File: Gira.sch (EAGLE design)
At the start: 20 parts, among them IC1 MEGA8-PTQFP

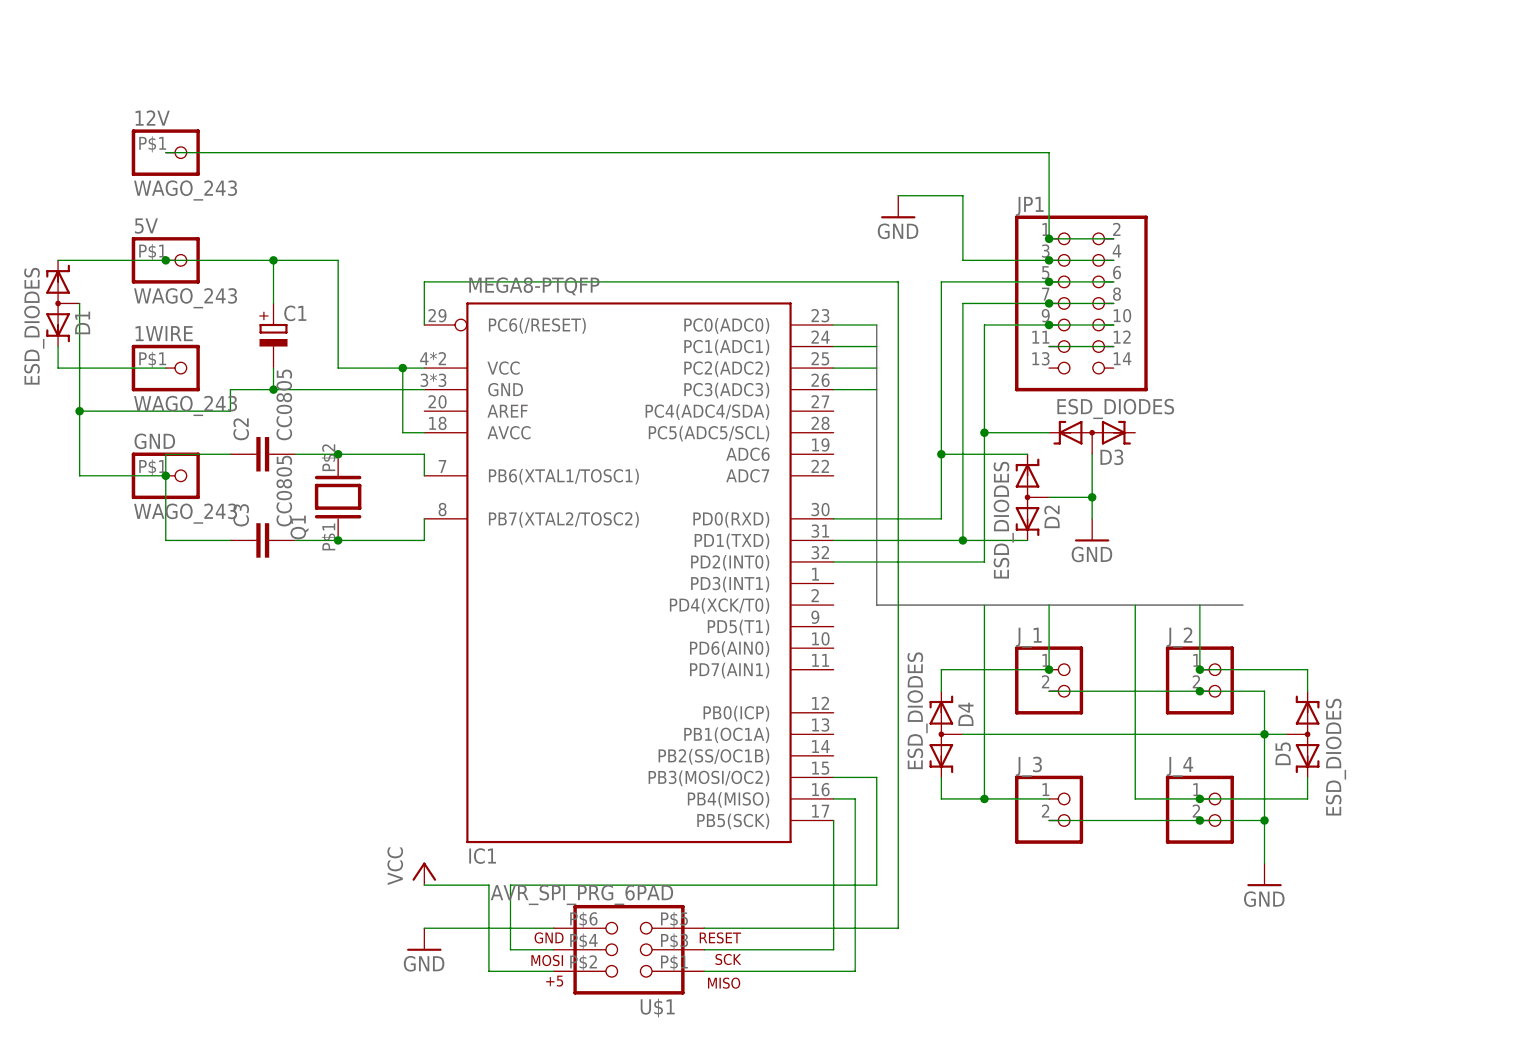
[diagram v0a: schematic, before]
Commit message: Additional ground, I²C bus, input for light measurement
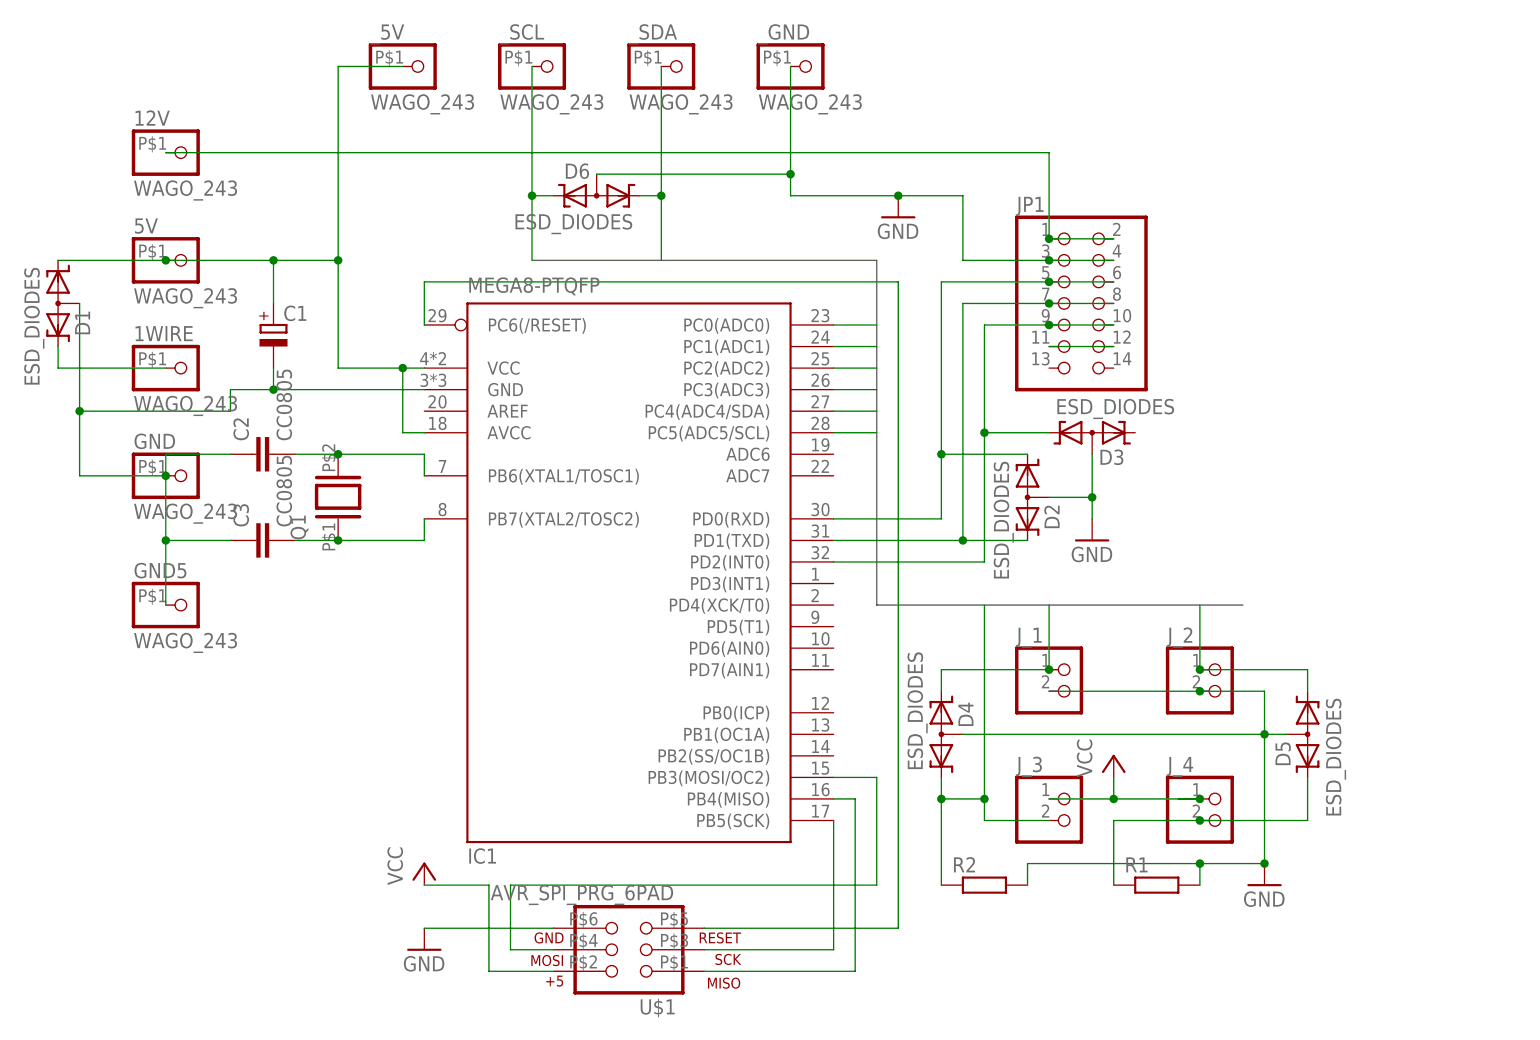
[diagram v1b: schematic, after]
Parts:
- added D6: ESD_DIODES, common:ESD_DIODES
- added GND5, _5V, _GND, _SCL, _SDA: WAGO_243, common:WAGO_243
- added R1, R2: (no value), resistor:R-EU_R0603
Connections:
- new net N$6: D5.K2, J_4.2, R1.1
- new net SCL: D6.K2, IC1.PC5(ADC5/SCL), _SCL.1
- new net SDA: D6.K1, IC1.PC4(ADC4/SDA), _SDA.1
- new net VCC: J_3.1, J_4.1
- net 5V: now also _5V.1
- net B3: now also J_3.2, R2.1; no longer J_3.1
- net B4: no longer D5.K2, J_4.1
- net GND: now also D6.AA, GND5.1, R1.2, R2.2, _GND.1; no longer J_3.2, J_4.2

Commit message: Update Gira
min 0.3mm
Klemmen gedreht
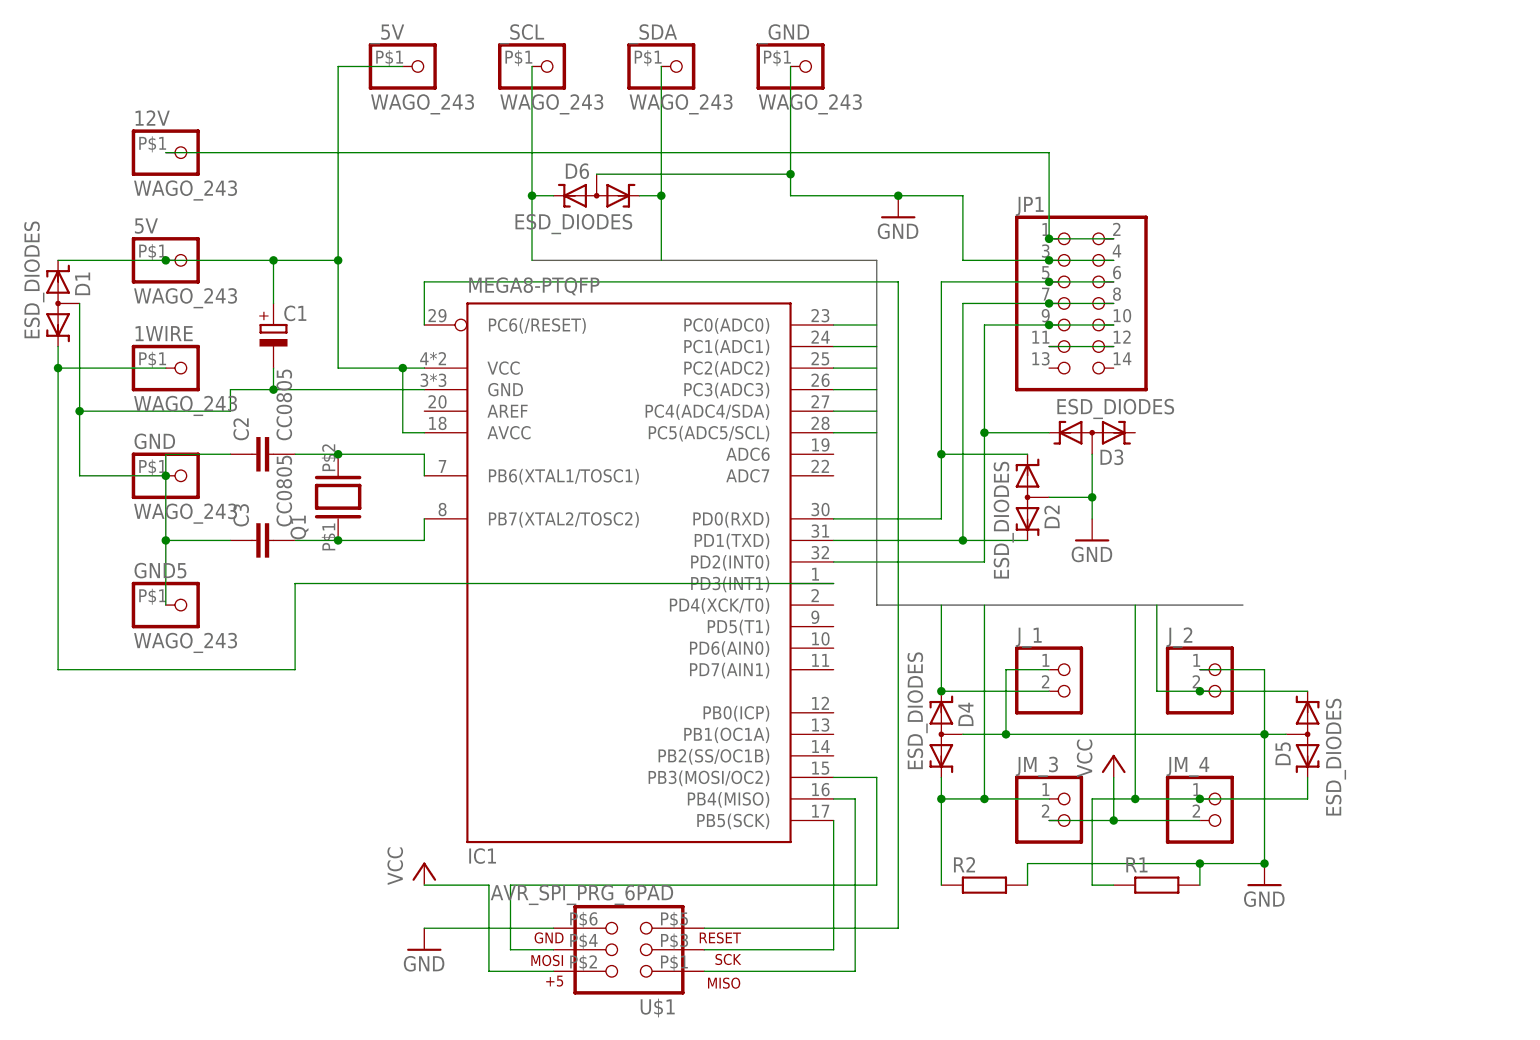
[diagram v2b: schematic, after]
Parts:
- removed J_3, J_4: (no value), pinhead:PINHD-1X2
- added JM_3, JM_4: (no value), common:PINHD-1X2LEVER
- J_1, J_2: device pinhead:PINHD-1X2 -> common:PINHD-1X2LEVER
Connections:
- removed net N$6: D5.K2, J_4.2, R1.1
- removed net VCC: J_3.1, J_4.1
- net 5V: now also D1.K2, JM_3.2, JM_4.2; no longer D1.K1
- net B1: now also J_1.2; no longer J_1.1
- net B2: now also J_2.2; no longer J_2.1
- net B3: now also JM_3.1; no longer J_3.2
- net B4: now also D5.K2, JM_4.1, R1.1
- net GND: now also J_1.1, J_2.1; no longer J_1.2, J_2.2
- net N$2: now also D1.K1, IC1.PD3(INT1); no longer D1.K2
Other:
- moved on the sheet: D1

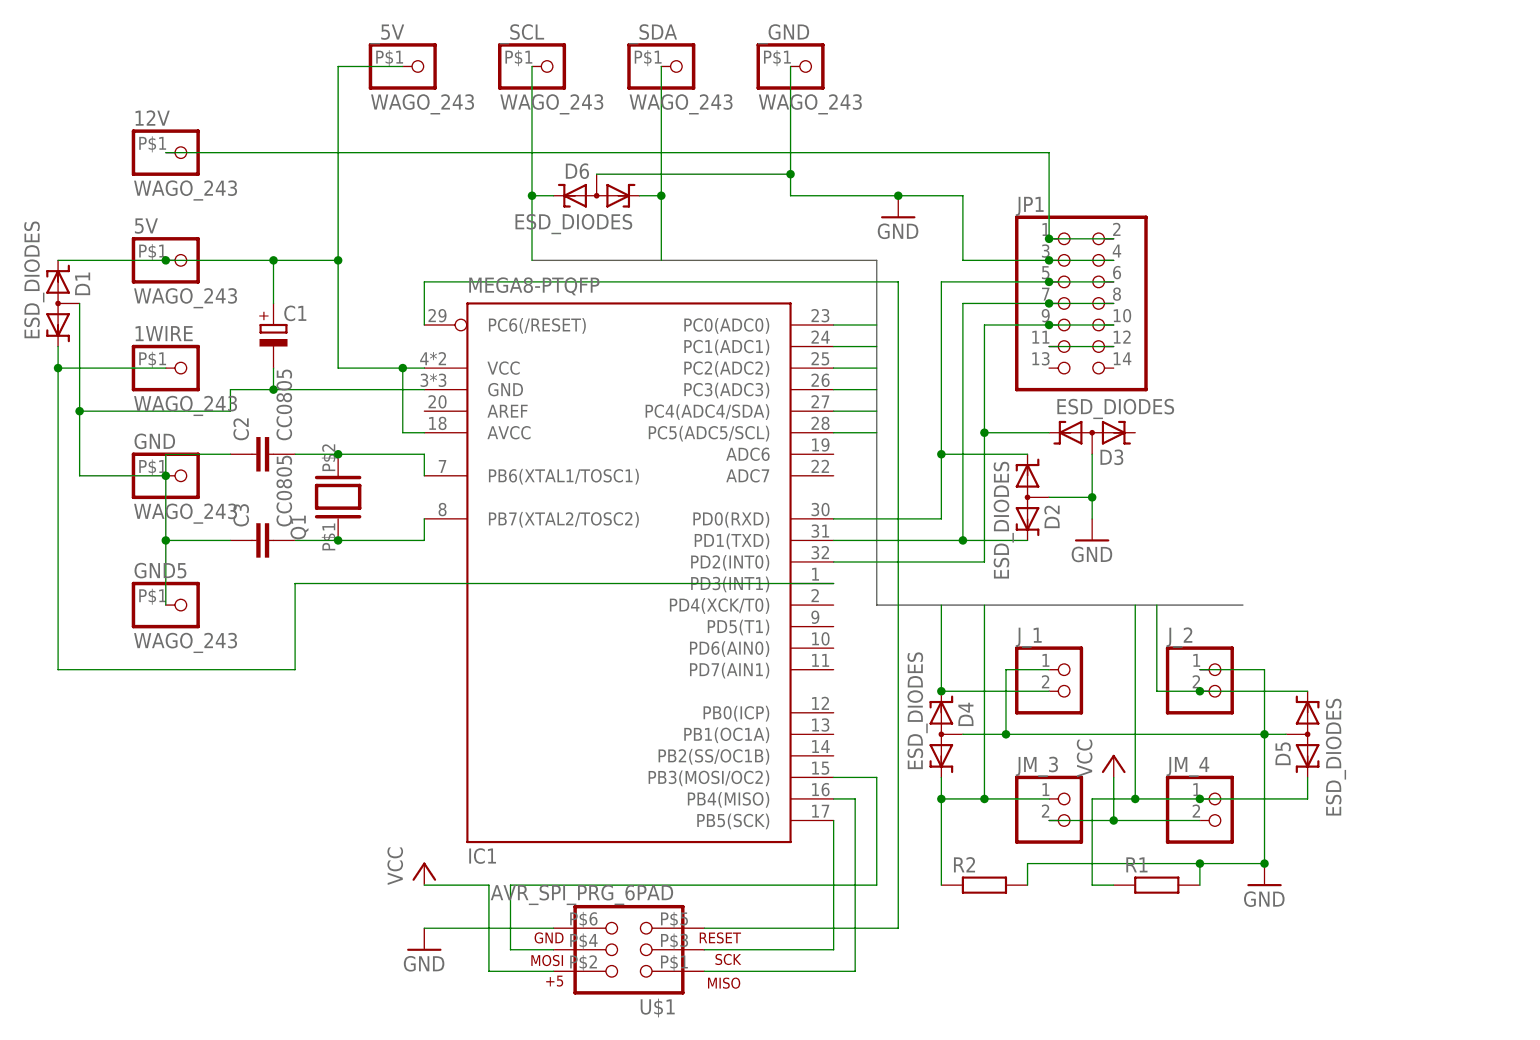
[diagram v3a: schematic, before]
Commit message: V2.1
* Umstellung auf 3.3V (aus dem Rauchmelder)
* keine Pullups am Port
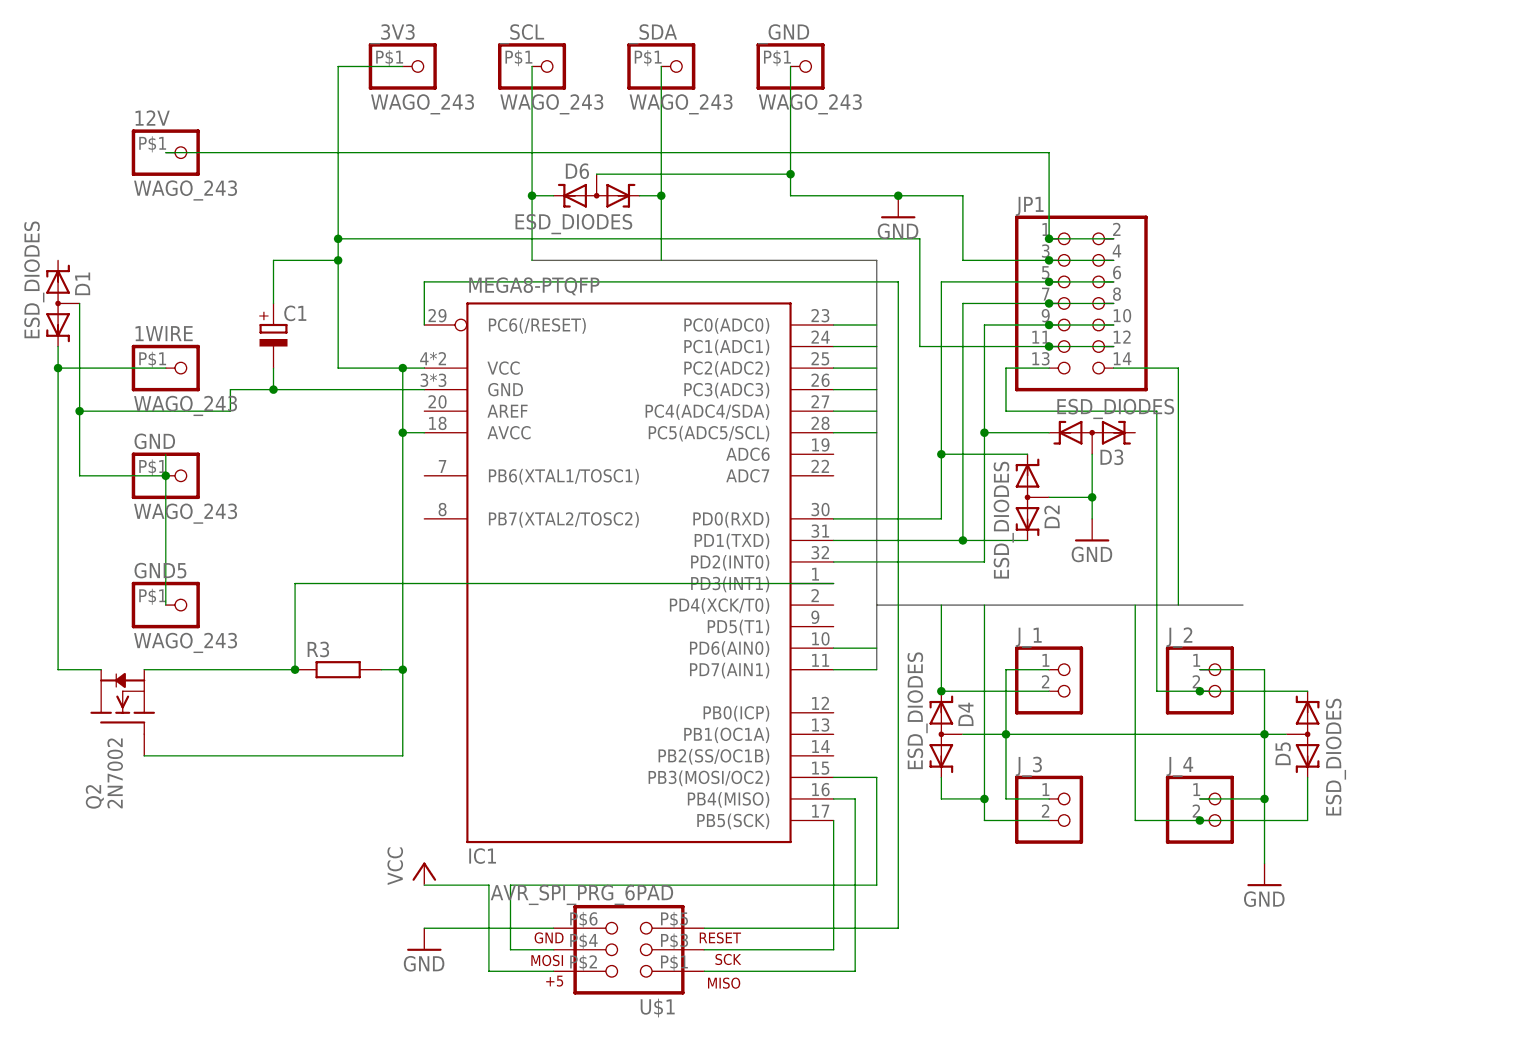
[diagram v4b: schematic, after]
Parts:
- removed 5V: WAGO_243, common:WAGO_243
- removed C2, C3: CC0805, common:CC0805
- removed Q1: (no value), common:XTALSMD5
- removed R1, R2: (no value), resistor:R-EU_R0603
- added Q2: 2N7002, common:2N7002
- added R3: (no value), common:R-EU_R0603
- renumbered JM_3 to J_3, JM_4 to J_4, _5V to _3V3
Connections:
- removed net N$17: JP1.11, JP1.12
- removed net N$4: C3.2, IC1.PB7(XTAL2/TOSC2), Q1.1
- removed net N$5: C2.2, IC1.PB6(XTAL1/TOSC1), Q1.2
- new net 3V3: C1.+, IC1.AVCC, IC1.VCC, JP1.11, JP1.12, Q2.G, R3.2, _3V3.1
- new net N$3: 1WIRE.1, D1.K1, Q2.D
- new net RESET: IC1.PD6(AIN0), JP1.13
- new net TEST: IC1.PD7(AIN1), JP1.14
- net 5V: no longer 5V.1, C1.+, D1.K2, IC1.AVCC, IC1.VCC, J_3.2, J_4.2, _3V3.1
- net B3: now also J_3.2; no longer J_3.1, R2.1
- net B4: now also J_4.2; no longer J_4.1, R1.1
- net GND: now also J_3.1, J_4.1; no longer C2.1, C3.1, R1.2, R2.2
- net N$2: now also Q2.S, R3.1; no longer 1WIRE.1, D1.K1
